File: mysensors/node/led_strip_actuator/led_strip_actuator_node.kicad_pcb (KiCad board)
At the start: 2 copper layers, 36.8 x 36.7 mm, 86 parts, among them CON1 AVR-ISP-6, IC1 ATMEGA328P, J1 CONN_01X02, J2 LED_BTN, P1 ANTENNA, Q1 MMBT2222, SW1 RESET, U1 AT25DF512C, U2 ATSHA204A, U3 AMS1117-3.3, U4 RFM69W, X1 LED_SW, X2 12V, Y1 8MHz

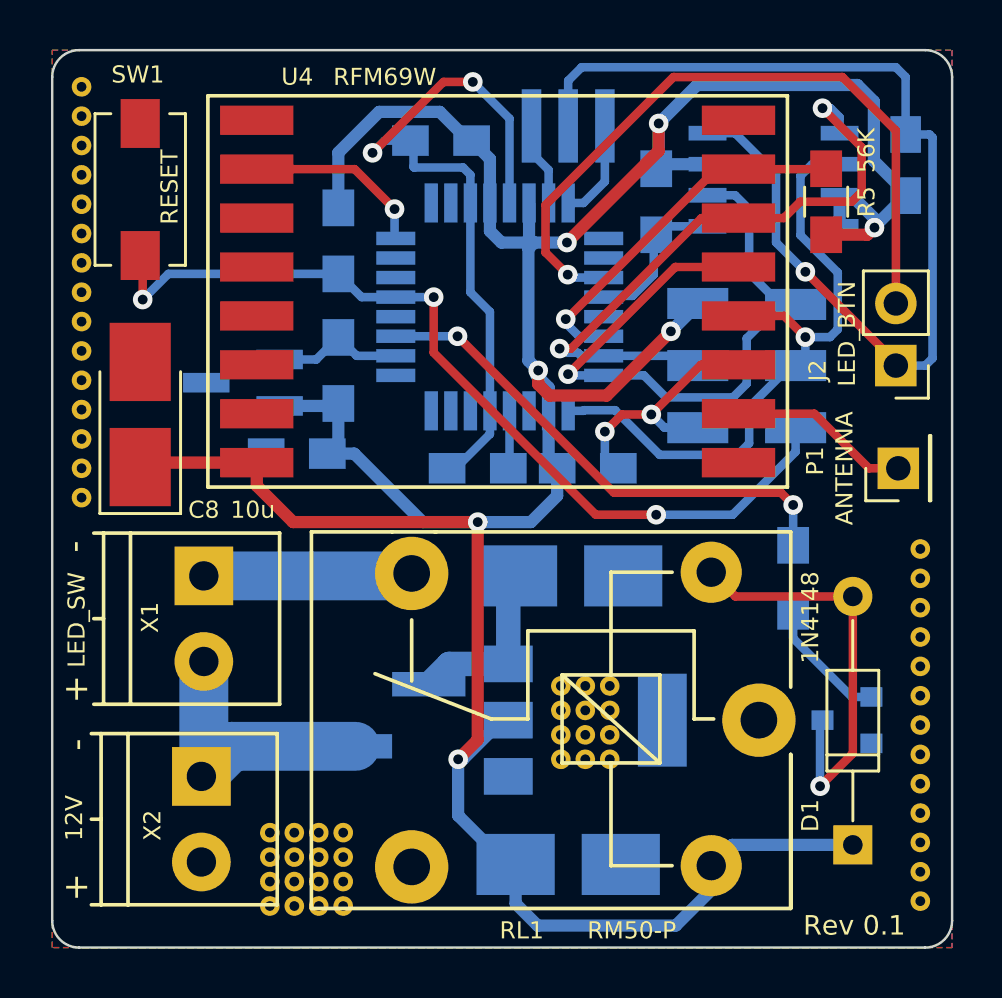
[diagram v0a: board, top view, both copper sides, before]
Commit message: [led_strip_actuator] pcb estetic refactorings
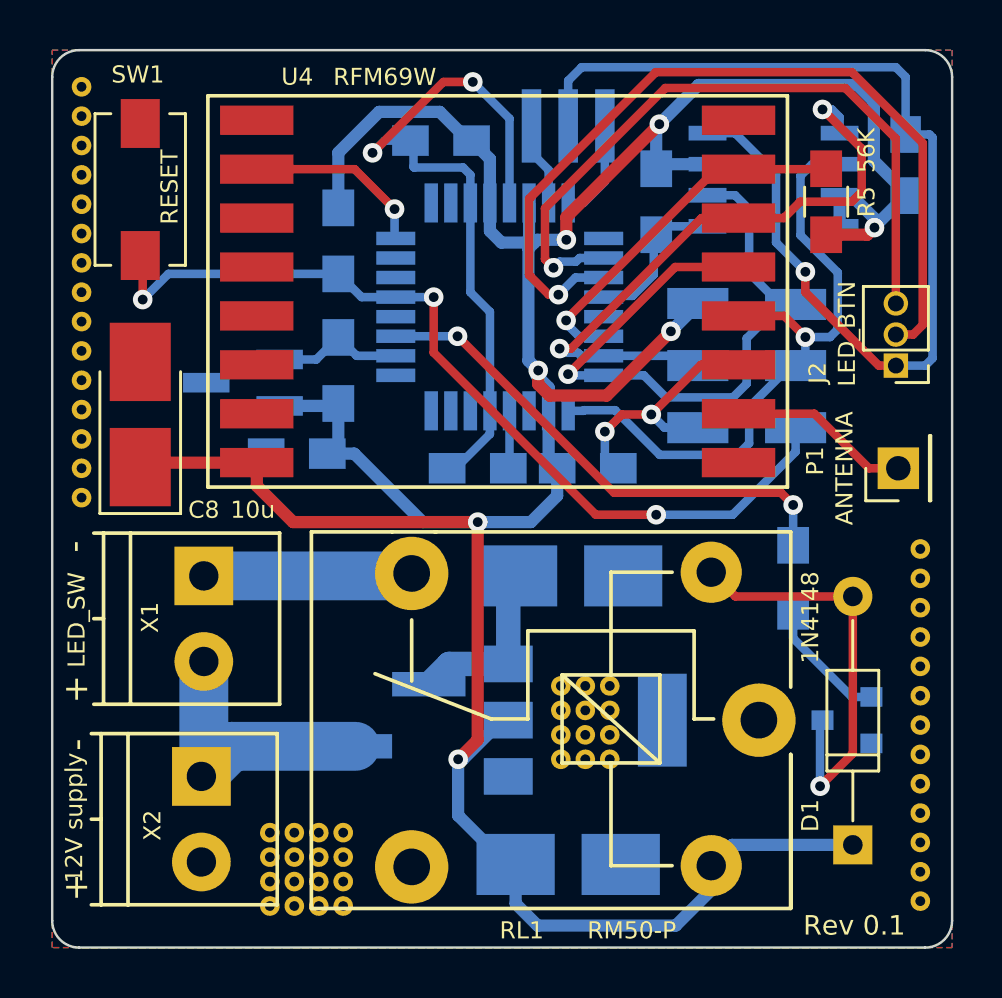
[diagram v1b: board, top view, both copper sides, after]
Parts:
- IC1: value ATMEGA328P -> ATMEGA328P-A
- J1: value CONN_01X02 -> EXT_DC_DC
- J2: footprint Pin_Headers:Pin_Header_Straight_1x02_Pitch2.54mm -> Pin_Headers:Pin_Header_Straight_1x03_Pitch1.27mm
- X2: value 12V -> 12V supply
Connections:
- IC1 pad 10: (no net) -> /LED_BTN_SIGNALING
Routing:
- net /LED_BTN_SIGNALING: track 0.00 -> 28.8 mm, vias 0 -> 1
- net /LED_BTN: track 29.2 -> 34.9 mm
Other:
- board text added: "BTN"
- board text added: "LED"

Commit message: [led_strip_actuator] added relay voltage selector jumpers
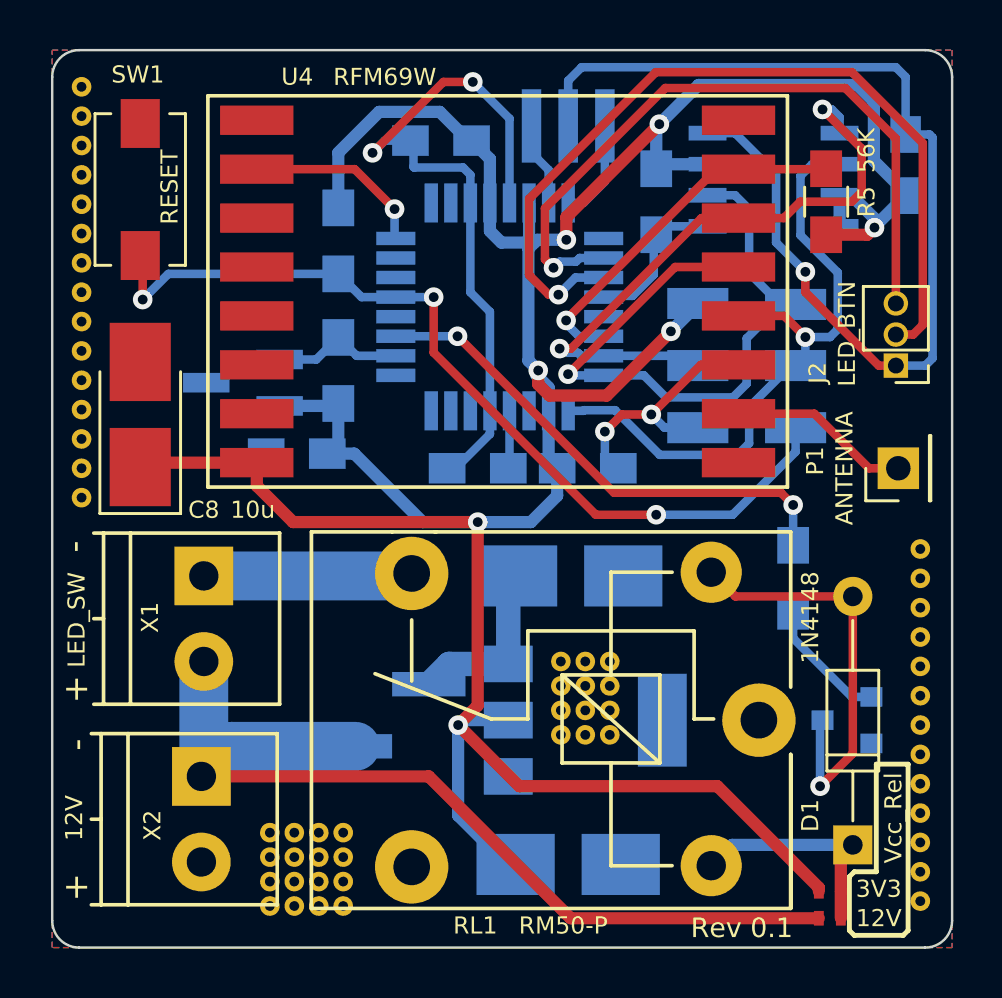
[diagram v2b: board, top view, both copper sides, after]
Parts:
- added JP1: 3V3, Resistors_SMD:R_0402_NoSilk, F.Cu at (143.0, 90.7)
- added JP2: 12V, Resistors_SMD:R_0402_NoSilk, F.Cu at (143.0, 91.8)
- IC1: value ATMEGA328P-A -> ATMEGA328P
- X2: value 12V supply -> 12V
- moved REF** 4.00 mm to (134.0, 81.3)
- moved REF** 4.00 mm to (133.0, 81.3)
- moved REF** 4.00 mm to (132.0, 81.3)
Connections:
- D1 pad 1: +3V3 -> Net-(D1-Pad1)
- RL1 pad A1: +3V3 -> Net-(D1-Pad1)
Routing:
- net /LED_12V: track 11.6 -> 39.2 mm
- net Net-(D1-Pad1): track 0.00 -> 9.35 mm
- net +3V3: track 136.8 -> 136.2 mm
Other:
- board text added: "Vcc_Rel"

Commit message: pcb refactorings
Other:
- board text added: "MySensors RFM69W LED Strip Actuator Node"
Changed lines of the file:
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@@
     (area 109.882143 48.027381 149.217857 95.2865)
     (thickness 1.6)
-    (drawings 33)
+    (drawings 34)
     (tracks 302)
     (zones 0)
@@
     (tags "Surface mounted pin header SMD 1x02 2.54mm single row style1 pin1 left")
     (attr smd)
-    (fp_text reference J1 (at 0 3.6) (layer B.SilkS)
+    (fp_text reference J1 (at -2.3 -1.7) (layer B.SilkS)
       (effects (font (size 0.7 0.7) (thickness 0.15)) (justify mirror))
     )
@@
     (descr "D, DO-35_SOD27 series, Axial, Horizontal, pin pitch=10.16mm, , length*diameter=4*2mm^2, , http://www.diodes.com/_files/packages/DO-35.pdf")
     (tags "D DO-35_SOD27 series Axial Horizontal pin pitch 10.16mm  length 4mm diameter 2mm")
-    (fp_text reference D1 (at 1.2 -1.74 90) (layer F.SilkS)
-      (effects (font (size 0.7 0.7) (thickness 0.15)))
-    )
-    (fp_text value 1N4148 (at 9.3 -1.74 90) (layer F.SilkS)
+    (fp_text reference D1 (at 6.5 1.76 90) (layer F.SilkS)
+      (effects (font (size 0.7 0.7) (thickness 0.15)))
+    )
+    (fp_text value 1N4148 (at 9.5 1.76 90) (layer F.SilkS)
       (effects (font (size 0.7 0.7) (thickness 0.15)))
     )
@@
     (at 140.1 83.7 180)
     (descr "relay, Sanyou SRD series Form C")
-    (fp_text reference RL1 (at 11.6 -8.4 180) (layer F.SilkS)
-      (effects (font (size 0.7 0.7) (thickness 0.15)))
-    )
-    (fp_text value RM50-P (at 8 -8.4 180) (layer F.SilkS)
+    (fp_text reference RL1 (at 13.3 8.5 180) (layer F.SilkS)
+      (effects (font (size 0.7 0.7) (thickness 0.15)))
+    )
+    (fp_text value RM50-P (at 8.5 8.5 180) (layer F.SilkS)
       (effects (font (size 0.7 0.7) (thickness 0.15)))
     )
@@
       (effects (font (size 0.7 0.7) (thickness 0.15)))
     )
-    (fp_text value LED_SW (at 1.8 5.2 270) (layer F.SilkS)
+    (fp_text value LED_SW (at 1.8 5.2 90) (layer F.SilkS)
       (effects (font (size 0.7 0.7) (thickness 0.15)))
     )
@@
       (effects (font (size 0.7 0.7) (thickness 0.15)))
     )
-    (fp_text value "12V " (at 1.7 5.2 270) (layer F.SilkS)
+    (fp_text value "12V " (at 1.7 5.2 90) (layer F.SilkS)
       (effects (font (size 0.7 0.7) (thickness 0.15)))
     )
@@
       (net 17 /LED_12V))
   )
+  (gr_text "MySensors RFM69W LED Strip Actuator Node" (at 128.7 92.2) (layer F.SilkS)
+    (effects (font (size 0.8 0.8) (thickness 0.15)))
+  )
   (gr_line (start 143.8 90.1) (end 143.8 90.1) (layer F.SilkS) (width 0.2))
   (gr_line (start 144 89.9) (end 143.8 90.1) (layer F.SilkS) (width 0.2))
@@
     (effects (font (size 0.7 0.7) (thickness 0.15)) (justify mirror))
   )
-  (gr_text "Rev 0.1" (at 139.4 92.2) (layer F.SilkS)
+  (gr_text "Rev 0.1" (at 146.6 59.7 90) (layer F.SilkS)
     (effects (font (size 0.8 0.8) (thickness 0.15)))
   )
